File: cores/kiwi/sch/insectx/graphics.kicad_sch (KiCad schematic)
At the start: 26 parts, among them U1 LH53400, U10 74LS374, U11 74LS04, U16 74LS157, U2 LH53400, U23 74LS245, U24-1 YM3906, U24-2 YM3909, U29 74LS32, U33 74LS245, U40 74LS245, U41 74LS374, U42 TMM2063AP_10, U45 X1-007, U48 74LS14, U50 X1-006, U54 74LS161, U9 74LS174

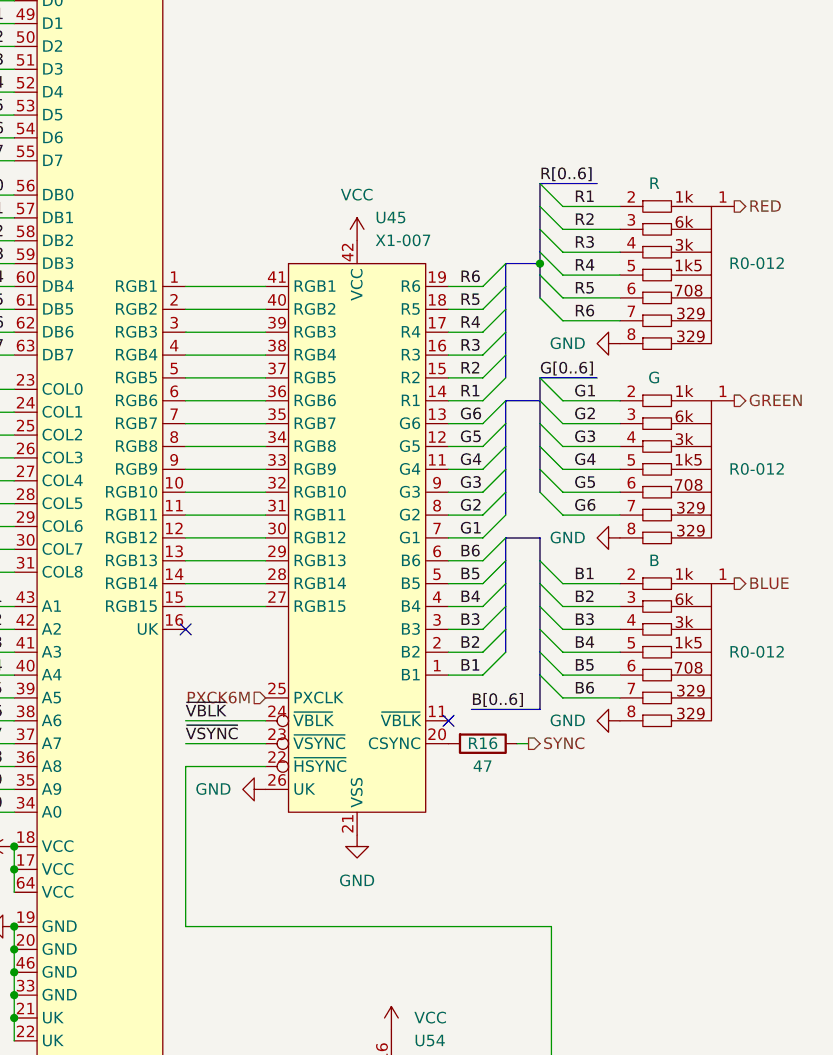
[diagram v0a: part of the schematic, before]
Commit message: updated schematics with correct pins names on the RGB output. As per [insectx] schematic signals #22
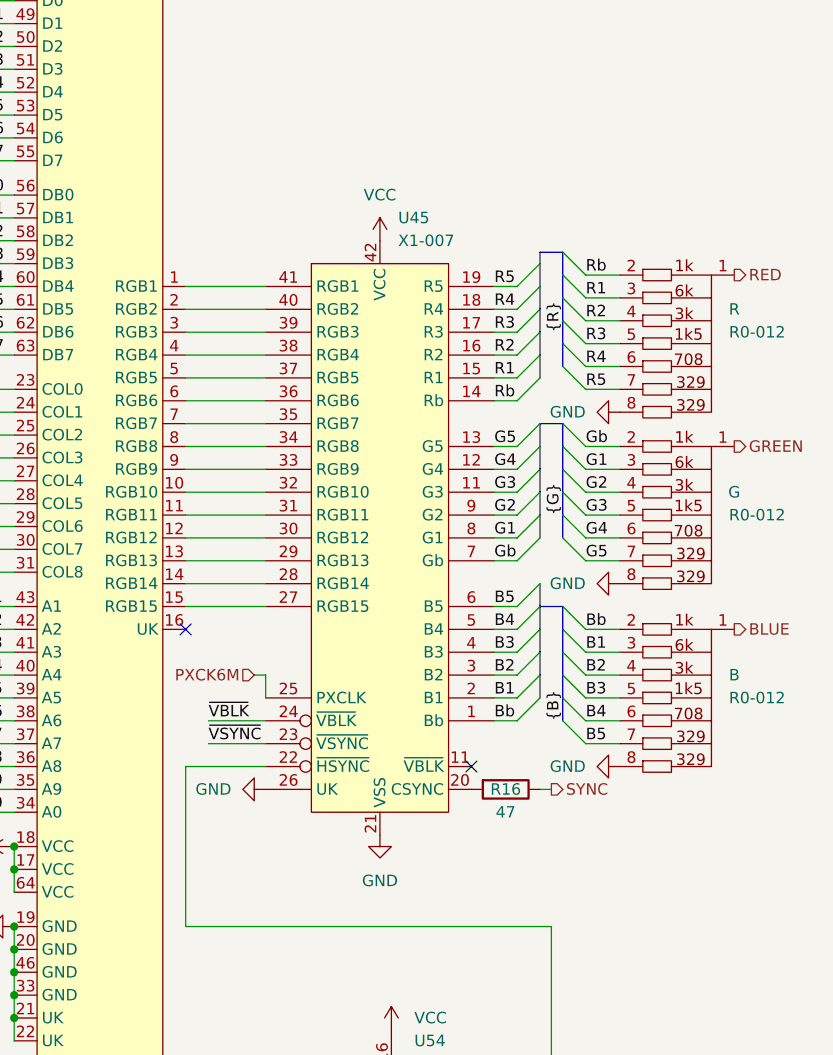
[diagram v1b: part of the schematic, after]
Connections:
- net B6 is gone; now on net B5: B1.7, U45.6 (B5)
- net G6 is gone; now on net G5: G1.7, U45.13 (G5)
- net R6 is gone; now on net R5: R999.7, U45.19 (R5)
- net B1: now also B1.3, U45.2 (B1); no longer B1.2, U45.1 (B1)
- net B2: now also B1.4, U45.3 (B2); no longer B1.3, U45.2 (B2)
- net B3: now also B1.5, U45.4 (B3); no longer B1.4, U45.3 (B3)
- net B4: now also B1.6, U45.5 (B4); no longer B1.5, U45.4 (B4)
- net B5: no longer B1.6, U45.5 (B5)
- net G1: now also G1.3, U45.8 (G1); no longer G1.2, U45.7 (G1)
- net G2: now also G1.4, U45.9 (G2); no longer G1.3, U45.8 (G2)
- net G3: now also G1.5, U45.11 (~{VBLK}); no longer G1.4, U45.9 (G3)
- net G4: now also G1.6, U45.12 (G4); no longer G1.5, U45.11 (~{VBLK})
- net G5: no longer G1.6, U45.12 (G5)
- net R1: now also R999.3, U45.15 (R1); no longer R999.2, U45.14 (R1)
- net R2: now also R999.4, U45.16 (R2); no longer R999.3, U45.15 (R2)
- net R3: now also R999.5, U45.17 (R3); no longer R999.4, U45.16 (R3)
- net R4: now also R999.6, U45.18 (R4); no longer R999.5, U45.17 (R4)
- net R5: no longer R999.6, U45.18 (R5)
- new net Bb: B1.2, U45.1 (Bb)
- new net Gb: G1.2, U45.7 (Gb)
- new net Rb: R999.2, U45.14 (Rb)
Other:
- moved on the sheet: R16, U45
